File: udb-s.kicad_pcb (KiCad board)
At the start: 4 copper layers, 40 x 9 mm, 11 parts, among them J1 TYPE-C-31-M-12, J2 78171-0004, U1 TPD4E05U06DQAR

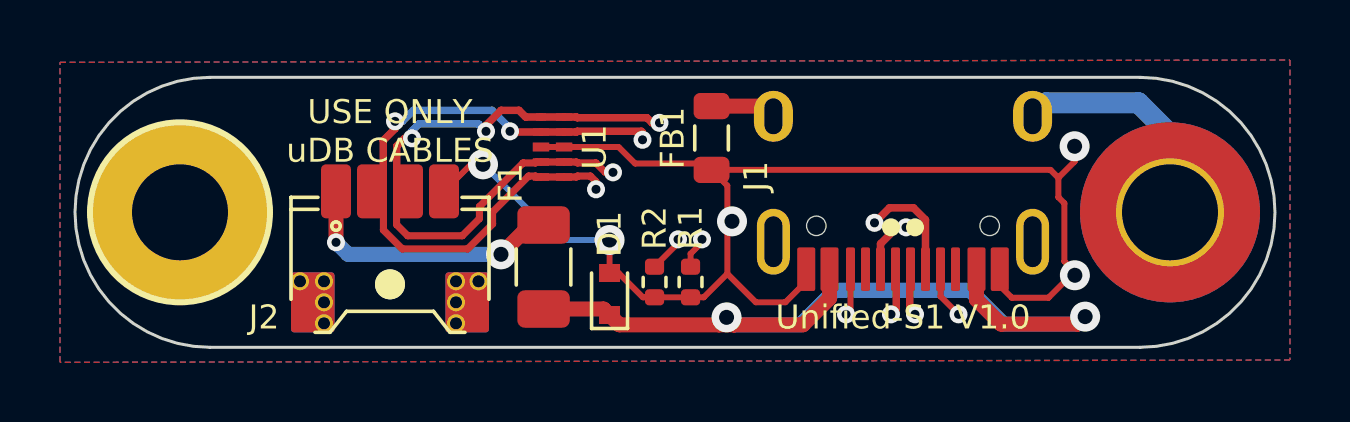
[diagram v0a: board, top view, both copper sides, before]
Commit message: added kikit panel assembly
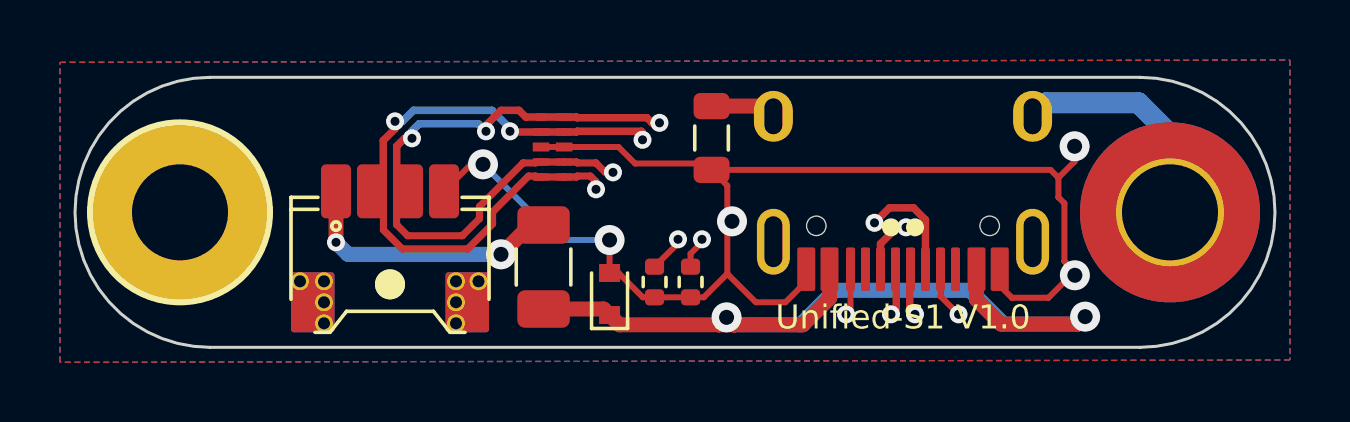
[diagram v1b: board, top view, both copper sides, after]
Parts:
- removed G***: LOGO, locallib:UnifiedLogo
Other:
- board text removed: "USE ONLY uDB CABLES"
- board text removed: "Unified-S1 V1.0 www.unified- daughterboard.github.io"
